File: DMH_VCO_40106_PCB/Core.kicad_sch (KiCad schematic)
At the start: 56 parts, among them Q1 BC558, Q2 BC548, U1 40106, U2 TL074, U3 TL074

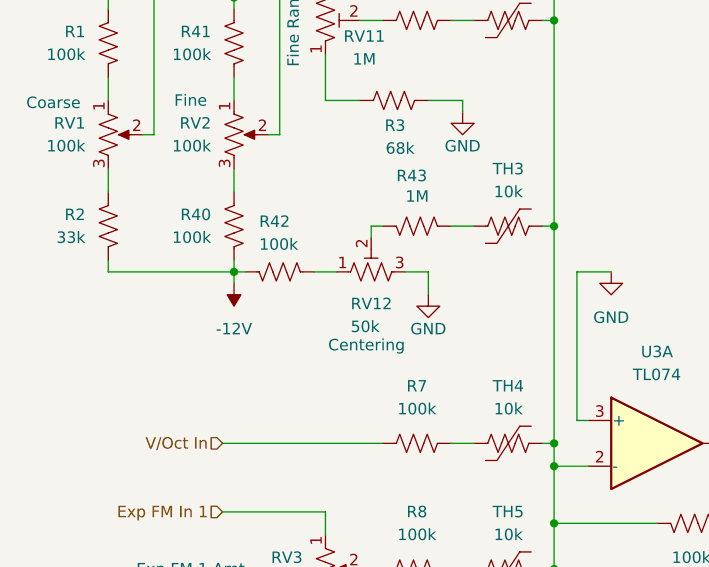
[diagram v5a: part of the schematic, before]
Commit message: Improved range of Coarse knob
... and allowed Centering knob to set C1=32,7Hz as root note with Coarse knob all the way CCW.
... and added 1kHz to Sine output.
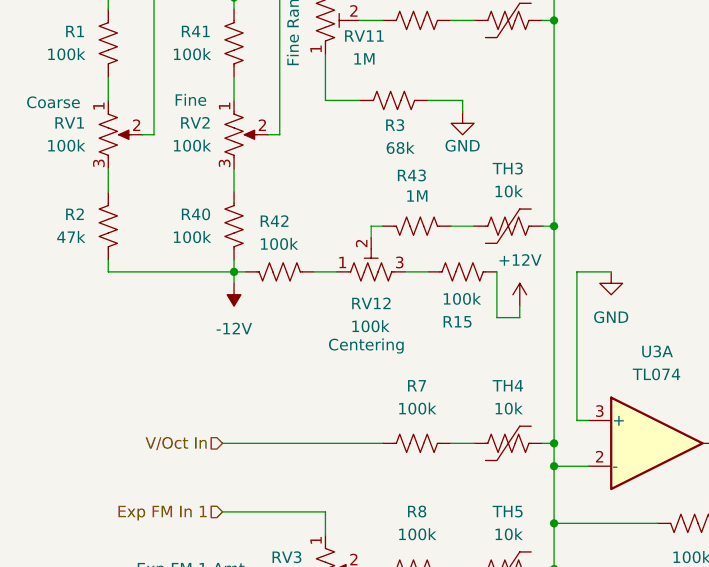
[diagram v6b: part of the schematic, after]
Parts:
- added R15: 100k, Resistor_THT:R_Axial_DIN0204_L3.6mm_D1.6mm_P5.08mm_Horizontal, symbol Device:R_US
- R2: value 33k -> 47k
- RV12: value 50k -> 100k
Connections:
- net +12V: now also R15.1
- net GND: no longer RV12.3
- new net: R15.2, RV12.3
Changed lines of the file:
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@@
 	(wire
 		(pts
+			(xy 66.04 88.9) (xy 66.04 93.98)
+		)
+		(stroke
+			(width 0)
+			(type default)
+		)
+	)
+	(wire
+		(pts
 			(xy 203.2 24.13) (xy 219.71 24.13)
 		)
@@
 	(wire
 		(pts
+			(xy 68.58 93.98) (xy 68.58 92.71)
+		)
+		(stroke
+			(width 0)
+			(type default)
+		)
+	)
+	(wire
+		(pts
 			(xy 237.49 39.37) (xy 237.49 26.67)
 		)
@@
 	(wire
 		(pts
-			(xy 58.42 88.9) (xy 58.42 91.44)
-		)
-		(stroke
-			(width 0)
-			(type default)
-		)
-	)
-	(wire
-		(pts
 			(xy 46.99 125.73) (xy 46.99 128.27)
 		)
@@
 	(wire
 		(pts
+			(xy 66.04 93.98) (xy 68.58 93.98)
+		)
+		(stroke
+			(width 0)
+			(type default)
+		)
+	)
+	(wire
+		(pts
 			(xy 171.45 69.85) (xy 182.88 69.85)
 		)
@@
 	)
 	(symbol
+		(lib_id "power:+12V")
+		(at 68.58 92.71 0)
+		(unit 1)
+		(exclude_from_sim no)
+		(in_bom yes)
+		(on_board yes)
+		(dnp no)
+		(fields_autoplaced yes)
+		(property "Reference" "#PWR02"
+			(at 68.58 96.52 0)
+			(effects
+				(font
+					(size 1.27 1.27)
+				)
+				(hide yes)
+			)
+		)
+		(property "Value" "+12V"
+			(at 68.58 87.63 0)
+			(effects
+				(font
+					(size 1.27 1.27)
+				)
+			)
+		)
+		(property "Footprint" ""
+			(at 68.58 92.71 0)
+			(effects
+				(font
+					(size 1.27 1.27)
+				)
+				(hide yes)
+			)
+		)
+		(property "Datasheet" ""
+			(at 68.58 92.71 0)
+			(effects
+				(font
+					(size 1.27 1.27)
+				)
+				(hide yes)
+			)
+		)
+		(property "Description" "Power symbol creates a global label with name \"+12V\""
+			(at 68.58 92.71 0)
+			(effects
+				(font
+					(size 1.27 1.27)
+				)
+				(hide yes)
+			)
+		)
+		(pin "1"
+		)
+		(instances
+			(project "DMH_VCO_40106_PCB"
+				(path "/fefed352-c100-4617-bbfb-c55e7427b122/681eb850-910f-47de-ab28-b72b47bdbc38"
+					(reference "#PWR02")
+					(unit 1)
+				)
+			)
+		)
+	)
+	(symbol
 		(lib_id "power:-12V")
 		(at 133.35 115.57 180)
@@
 			)
 		)
-		(property "Value" "33k"
+		(property "Value" "47k"
 			(at 20.32 85.0899 0)
 			(effects
@@
 	)
 	(symbol
+		(lib_id "Device:R_US")
+		(at 62.23 88.9 270)
+		(unit 1)
+		(exclude_from_sim no)
+		(in_bom yes)
+		(on_board yes)
+		(dnp no)
+		(property "Reference" "R15"
+			(at 59.944 94.488 90)
+			(effects
+				(font
+					(size 1.27 1.27)
+				)
+				(justify left)
+			)
+		)
+		(property "Value" "100k"
+			(at 59.944 91.948 90)
+			(effects
+				(font
+					(size 1.27 1.27)
+				)
+				(justify left)
+			)
+		)
+		(property "Footprint" "Resistor_THT:R_Axial_DIN0204_L3.6mm_D1.6mm_P5.08mm_Horizontal"
+			(at 61.976 89.916 90)
+			(effects
+				(font
+					(size 1.27 1.27)
+				)
+				(hide yes)
+			)
+		)
+		(property "Datasheet" "~"
+			(at 62.23 88.9 0)
+			(effects
+				(font
+					(size 1.27 1.27)
+				)
+				(hide yes)
+			)
+		)
+		(property "Description" "Resistor, US symbol"
+			(at 62.23 88.9 0)
+			(effects
+				(font
+					(size 1.27 1.27)
+				)
+				(hide yes)
+			)
+		)
+		(pin "2"
+		)
+		(pin "1"
+		)
+		(instances
+			(project "DMH_VCO_40106_PCB"
+				(path "/fefed352-c100-4617-bbfb-c55e7427b122/681eb850-910f-47de-ab28-b72b47bdbc38"
+					(reference "R15")
+					(unit 1)
+				)
+			)
+		)
+	)
+	(symbol
 		(lib_id "Device:C")
 		(at 157.48 109.22 0)
@@
 			)
 		)
-		(property "Value" "50k"
+		(property "Value" "100k"
 			(at 49.784 94.996 90)
 			(effects
@@
 					(unit 1)
 				)
-			)
-		)
-	)
-	(symbol
-		(lib_id "power:GND")
-		(at 58.42 91.44 0)
-		(unit 1)
-		(exclude_from_sim no)
-		(in_bom yes)
-		(on_board yes)
-		(dnp no)
-		(property "Reference" "#PWR043"
-			(at 58.42 97.79 0)
-			(effects
-				(font
-					(size 1.27 1.27)
-				)
-				(hide yes)
-			)
-		)
-		(property "Value" "GND"
-			(at 58.42 95.25 0)
-			(effects
-				(font
-					(size 1.27 1.27)
-				)
-			)
-		)
-		(property "Footprint" ""
-			(at 58.42 91.44 0)
-			(effects
-				(font
-					(size 1.27 1.27)
-				)
-				(hide yes)
-			)
-		)
-		(property "Datasheet" ""
-			(at 58.42 91.44 0)
-			(effects
-				(font
-					(size 1.27 1.27)
-				)
-				(hide yes)
-			)
-		)
-		(property "Description" "Power symbol creates a global label with name \"GND\" , ground"
-			(at 58.42 91.44 0)
-			(effects
-				(font
-					(size 1.27 1.27)
-				)
-				(hide yes)
-			)
-		)
-		(pin "1"
-		)
-		(instances
-			(project "DMH_VCO_40106_PCB"
-				(path "/fefed352-c100-4617-bbfb-c55e7427b122/681eb850-910f-47de-ab28-b72b47bdbc38"
-					(reference "#PWR043")
-					(unit 1)
-				)

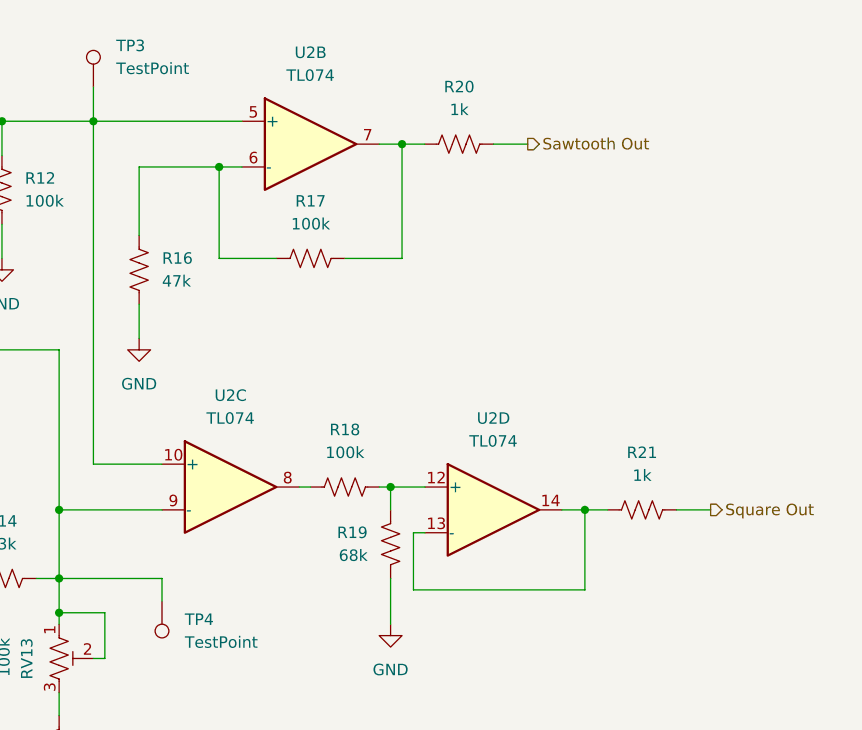
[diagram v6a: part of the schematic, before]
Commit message: Adjusted all output gains to 10Vpp
... and added buffer stages for Sawtooth Out and Triangle Out in order to avoid modifying Triangle and Sine wafeform characteristics when connecting Sawtooth Out and Triangle Out to other modules.
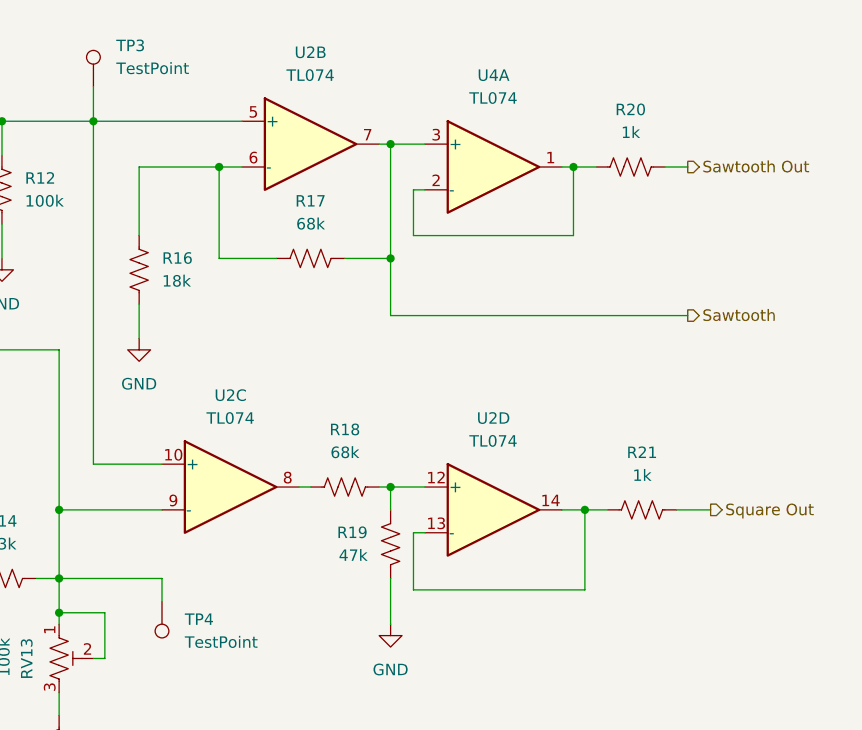
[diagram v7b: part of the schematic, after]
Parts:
- added U4: TL074, symbol Amplifier_Operational:TL074
- R16: value 47k -> 18k
- R17, R18: value 100k -> 68k
- R19: value 68k -> 47k
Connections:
- net Sawtooth: now reaches R17.1, U2.7
- net Sawtooth: now also U4.3 (+); no longer R20.2
- new net: R20.2, U4.1, U4.2 (-)
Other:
- moved on the sheet: R20
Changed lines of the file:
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@@
 	)
 	(junction
-		(at 237.49 26.67)
-		(diameter 0)
-		(color 0 0 0 0)
-	)
-	(junction
 		(at 72.39 83.82)
 		(diameter 0)
@@
 	)
 	(junction
+		(at 256.54 29.21)
+		(diameter 0)
+		(color 0 0 0 0)
+	)
+	(junction
 		(at 157.48 86.36)
 		(diameter 0)
@@
 	)
 	(junction
+		(at 236.22 39.37)
+		(diameter 0)
+		(color 0 0 0 0)
+	)
+	(junction
 		(at 199.39 74.93)
 		(diameter 0)
@@
 	)
 	(junction
+		(at 236.22 26.67)
+		(diameter 0)
+		(color 0 0 0 0)
+	)
+	(junction
 		(at 257.81 67.31)
 		(diameter 0)
@@
 	(wire
 		(pts
-			(xy 231.14 39.37) (xy 237.49 39.37)
+			(xy 231.14 39.37) (xy 236.22 39.37)
 		)
 		(stroke
@@
 	(wire
 		(pts
+			(xy 255.27 29.21) (xy 256.54 29.21)
+		)
+		(stroke
+			(width 0)
+			(type default)
+		)
+	)
+	(wire
+		(pts
 			(xy 101.6 88.9) (xy 106.68 88.9)
 		)
@@
 	(wire
 		(pts
-			(xy 237.49 39.37) (xy 237.49 26.67)
+			(xy 236.22 39.37) (xy 236.22 26.67)
 		)
 		(stroke
@@
 	(wire
 		(pts
-			(xy 170.18 49.53) (xy 175.26 49.53)
+			(xy 266.7 29.21) (xy 269.24 29.21)
 		)
 		(stroke
@@
 	(wire
 		(pts
-			(xy 247.65 26.67) (xy 251.46 26.67)
+			(xy 256.54 36.83) (xy 238.76 36.83)
 		)
 		(stroke
@@
 	(wire
 		(pts
-			(xy 234.95 26.67) (xy 237.49 26.67)
+			(xy 170.18 49.53) (xy 175.26 49.53)
+		)
+		(stroke
+			(width 0)
+			(type default)
+		)
+	)
+	(wire
+		(pts
+			(xy 234.95 26.67) (xy 236.22 26.67)
 		)
 		(stroke
@@
 	(wire
 		(pts
+			(xy 238.76 31.75) (xy 240.03 31.75)
+		)
+		(stroke
+			(width 0)
+			(type default)
+		)
+	)
+	(wire
+		(pts
 			(xy 160.02 30.48) (xy 180.34 30.48)
 		)
@@
 	(wire
 		(pts
+			(xy 236.22 45.72) (xy 236.22 39.37)
+		)
+		(stroke
+			(width 0)
+			(type default)
+		)
+	)
+	(wire
+		(pts
 			(xy 199.39 74.93) (xy 210.82 74.93)
 		)
@@
 	(wire
 		(pts
+			(xy 256.54 29.21) (xy 256.54 36.83)
+		)
+		(stroke
+			(width 0)
+			(type default)
+		)
+	)
+	(wire
+		(pts
 			(xy 35.56 107.95) (xy 53.34 107.95)
 		)
@@
 	(wire
 		(pts
-			(xy 237.49 26.67) (xy 240.03 26.67)
+			(xy 162.56 26.67) (xy 160.02 26.67)
 		)
 		(stroke
@@
 	(wire
 		(pts
-			(xy 162.56 26.67) (xy 160.02 26.67)
+			(xy 72.39 107.95) (xy 72.39 110.49)
 		)
 		(stroke
@@
 	(wire
 		(pts
-			(xy 72.39 107.95) (xy 72.39 110.49)
+			(xy 185.42 49.53) (xy 199.39 49.53)
 		)
 		(stroke
@@
 	(wire
 		(pts
-			(xy 185.42 49.53) (xy 199.39 49.53)
+			(xy 139.7 100.33) (xy 139.7 107.95)
 		)
 		(stroke
@@
 	(wire
 		(pts
-			(xy 139.7 100.33) (xy 139.7 107.95)
+			(xy 22.86 87.63) (xy 22.86 88.9)
 		)
 		(stroke
@@
 	(wire
 		(pts
-			(xy 22.86 87.63) (xy 22.86 88.9)
+			(xy 60.96 83.82) (xy 63.5 83.82)
 		)
 		(stroke
@@
 	(wire
 		(pts
-			(xy 60.96 83.82) (xy 63.5 83.82)
+			(xy 199.39 97.79) (xy 199.39 99.06)
 		)
 		(stroke
@@
 	(wire
 		(pts
-			(xy 199.39 97.79) (xy 199.39 99.06)
+			(xy 256.54 29.21) (xy 259.08 29.21)
 		)
 		(stroke
@@
 	(wire
 		(pts
+			(xy 238.76 36.83) (xy 238.76 31.75)
+		)
+		(stroke
+			(width 0)
+			(type default)
+		)
+	)
+	(wire
+		(pts
 			(xy 41.91 54.61) (xy 41.91 73.66)
 		)
@@
 	(wire
 		(pts
+			(xy 236.22 45.72) (xy 269.24 45.72)
+		)
+		(stroke
+			(width 0)
+			(type default)
+		)
+	)
+	(wire
+		(pts
 			(xy 199.39 49.53) (xy 199.39 67.31)
 		)
@@
 	(wire
 		(pts
+			(xy 236.22 26.67) (xy 240.03 26.67)
+		)
+		(stroke
+			(width 0)
+			(type default)
+		)
+	)
+	(wire
+		(pts
 			(xy 71.12 48.26) (xy 72.39 48.26)
 		)
@@
 		)
 	)
+	(hierarchical_label "Sawtooth"
+		(shape output)
+		(at 269.24 45.72 0)
+		(fields_autoplaced yes)
+		(effects
+			(font
+				(size 1.27 1.27)
+			)
+			(justify left)
+		)
+	)
 	(hierarchical_label "Exp FM In 1"
 		(shape input)
@@
 	(hierarchical_label "Sawtooth Out"
 		(shape output)
-		(at 251.46 26.67 0)
+		(at 269.24 29.21 0)
 		(fields_autoplaced yes)
 		(effects
@@
 			)
 		)
-		(property "Value" "68k"
+		(property "Value" "47k"
 			(at 233.68 72.3899 0)
 			(effects
@@
 	)
 	(symbol
+		(lib_id "Amplifier_Operational:TL074")
+		(at 247.65 29.21 0)
+		(unit 1)
+		(exclude_from_sim no)
+		(in_bom yes)
+		(on_board yes)
+		(dnp no)
+		(fields_autoplaced yes)
+		(property "Reference" "U4"
+			(at 247.65 19.05 0)
+			(effects
+				(font
+					(size 1.27 1.27)
+				)
+			)
+		)
+		(property "Value" "TL074"
+			(at 247.65 21.59 0)
+			(effects
+				(font
+					(size 1.27 1.27)
+				)
+			)
+		)
+		(property "Footprint" ""
+			(at 246.38 26.67 0)
+			(effects
+				(font
+					(size 1.27 1.27)
+				)
+				(hide yes)
+			)
+		)
+		(property "Datasheet" "http://www.ti.com/lit/ds/symlink/tl071.pdf"
+			(at 248.92 24.13 0)
+			(effects
+				(font
+					(size 1.27 1.27)
+				)
+				(hide yes)
+			)
+		)
+		(property "Description" "Quad Low-Noise JFET-Input Operational Amplifiers, DIP-14/SOIC-14"
+			(at 247.65 29.21 0)
+			(effects
+				(font
+					(size 1.27 1.27)
+				)
+				(hide yes)
+			)
+		)
+		(pin "7"
+		)
+		(pin "6"
+		)
+		(pin "5"
+		)
+		(pin "9"
+		)
+		(pin "1"
+		)
+		(pin "12"
+		)
+		(pin "2"
+		)
+		(pin "3"
+		)
+		(pin "11"
+		)
+		(pin "4"
+		)
+		(pin "8"
+		)
+		(pin "13"
+		)
+		(pin "10"
+		)
+		(pin "14"
+		)
+		(instances
+			(project ""
+				(path "/fefed352-c100-4617-bbfb-c55e7427b122/681eb850-910f-47de-ab28-b72b47bdbc38"
+					(reference "U4")
+					(unit 1)
+				)
+			)
+		)
+	)
+	(symbol
 		(lib_id "Device:R_US")
 		(at 57.15 107.95 90)
@@
 			)
 		)
-		(property "Value" "100k"
+		(property "Value" "68k"
 			(at 227.33 35.56 90)
 			(effects
@@
 			)
 		)
-		(property "Value" "47k"
+		(property "Value" "18k"
 			(at 210.82 41.9099 0)
 			(effects
@@
 	(symbol
 		(lib_id "Device:R_US")
-		(at 243.84 26.67 270)
+		(at 262.89 29.21 270)
 		(unit 1)
 		(exclude_from_sim no)
@@
 		(fields_autoplaced yes)
 		(property "Reference" "R20"
-			(at 243.84 20.32 90)
+			(at 262.89 22.86 90)
 			(effects
 				(font
@@
 		)
 		(property "Value" "1k"
-			(at 243.84 22.86 90)
+			(at 262.89 25.4 90)
 			(effects
 				(font
@@
 		)
 		(property "Footprint" "Resistor_THT:R_Axial_DIN0204_L3.6mm_D1.6mm_P5.08mm_Horizontal"
-			(at 243.586 27.686 90)
+			(at 262.636 30.226 90)
 			(effects
 				(font
@@
 		)
 		(property "Datasheet" "~"
-			(at 243.84 26.67 0)
+			(at 262.89 29.21 0)
 			(effects
 				(font
@@
 		)
 		(property "Description" "Resistor, US symbol"
-			(at 243.84 26.67 0)
+			(at 262.89 29.21 0)
 			(effects
 				(font
@@
 			)
 		)
-		(property "Value" "100k"
+		(property "Value" "68k"
 			(at 231.14 60.96 90)
 			(effects
